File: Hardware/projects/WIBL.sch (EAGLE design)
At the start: 105 parts, among them T2 S8050, T3 S8050, T4 S8050, U1 ESP32-WROOM-32E, U2 TJA1051T/3, U3 LSM6DS3TR-C, U4 AMS1117-3.3, U5 SN65C1168NSR

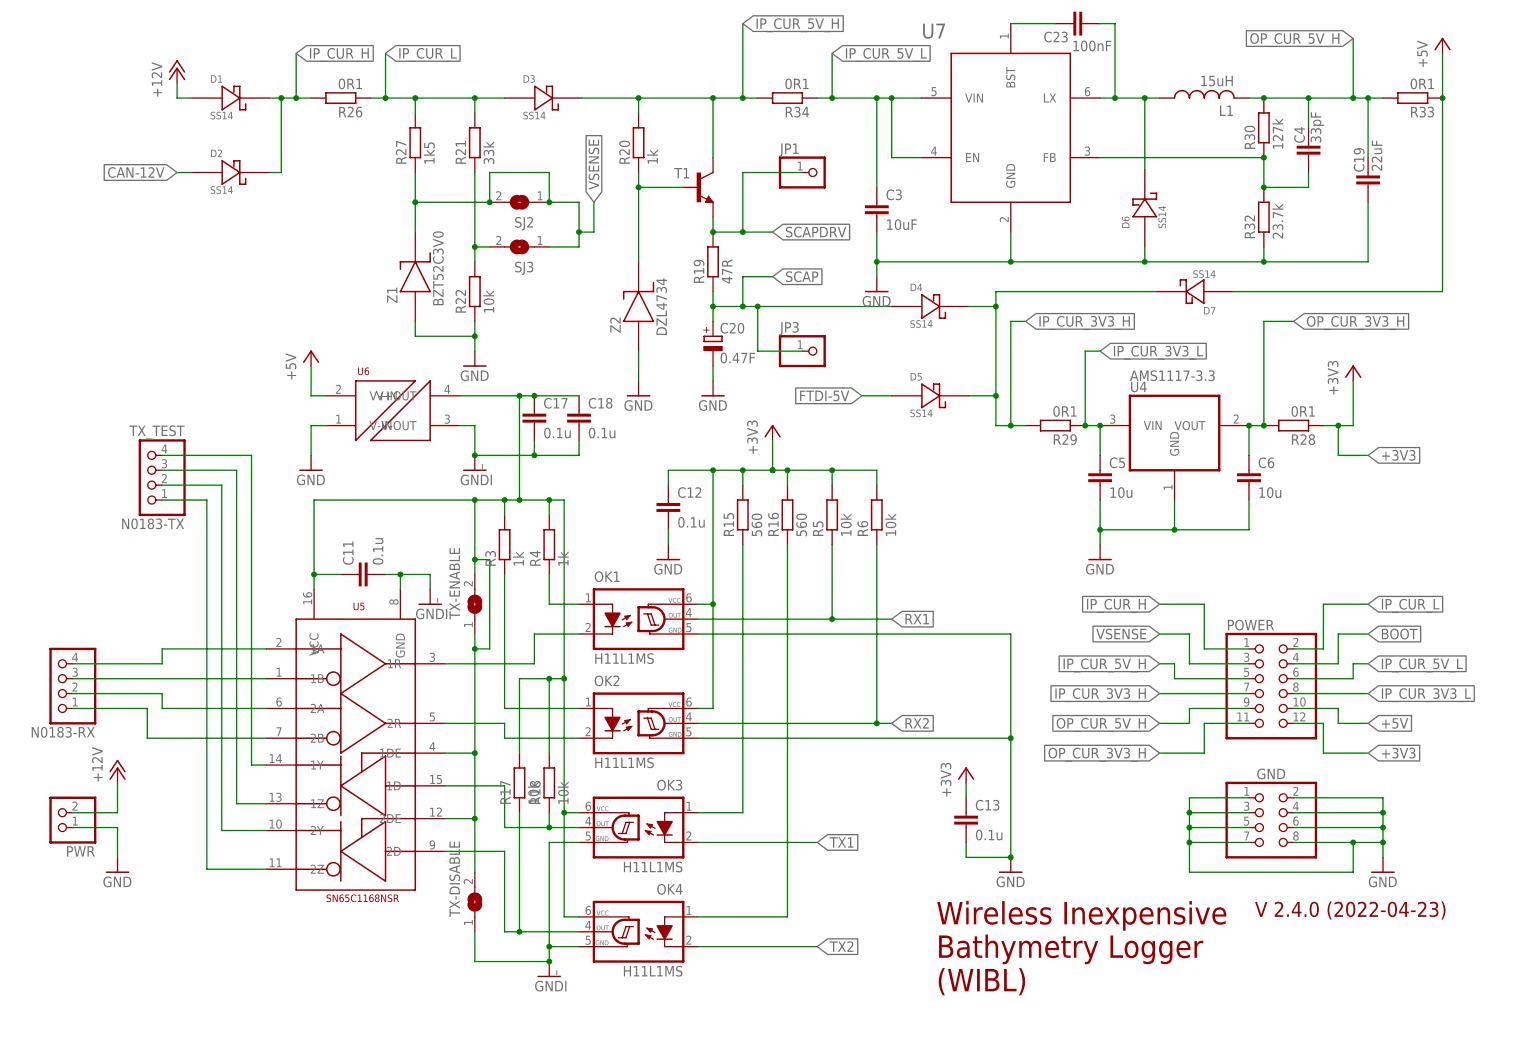
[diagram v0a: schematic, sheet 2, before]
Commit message: Added missing 2.4.1 hardware design files.
For reasons unknown, the v 2.4.1 schematic and board files never got checked into the repository; these are from a backup copy that reflects the initial state.
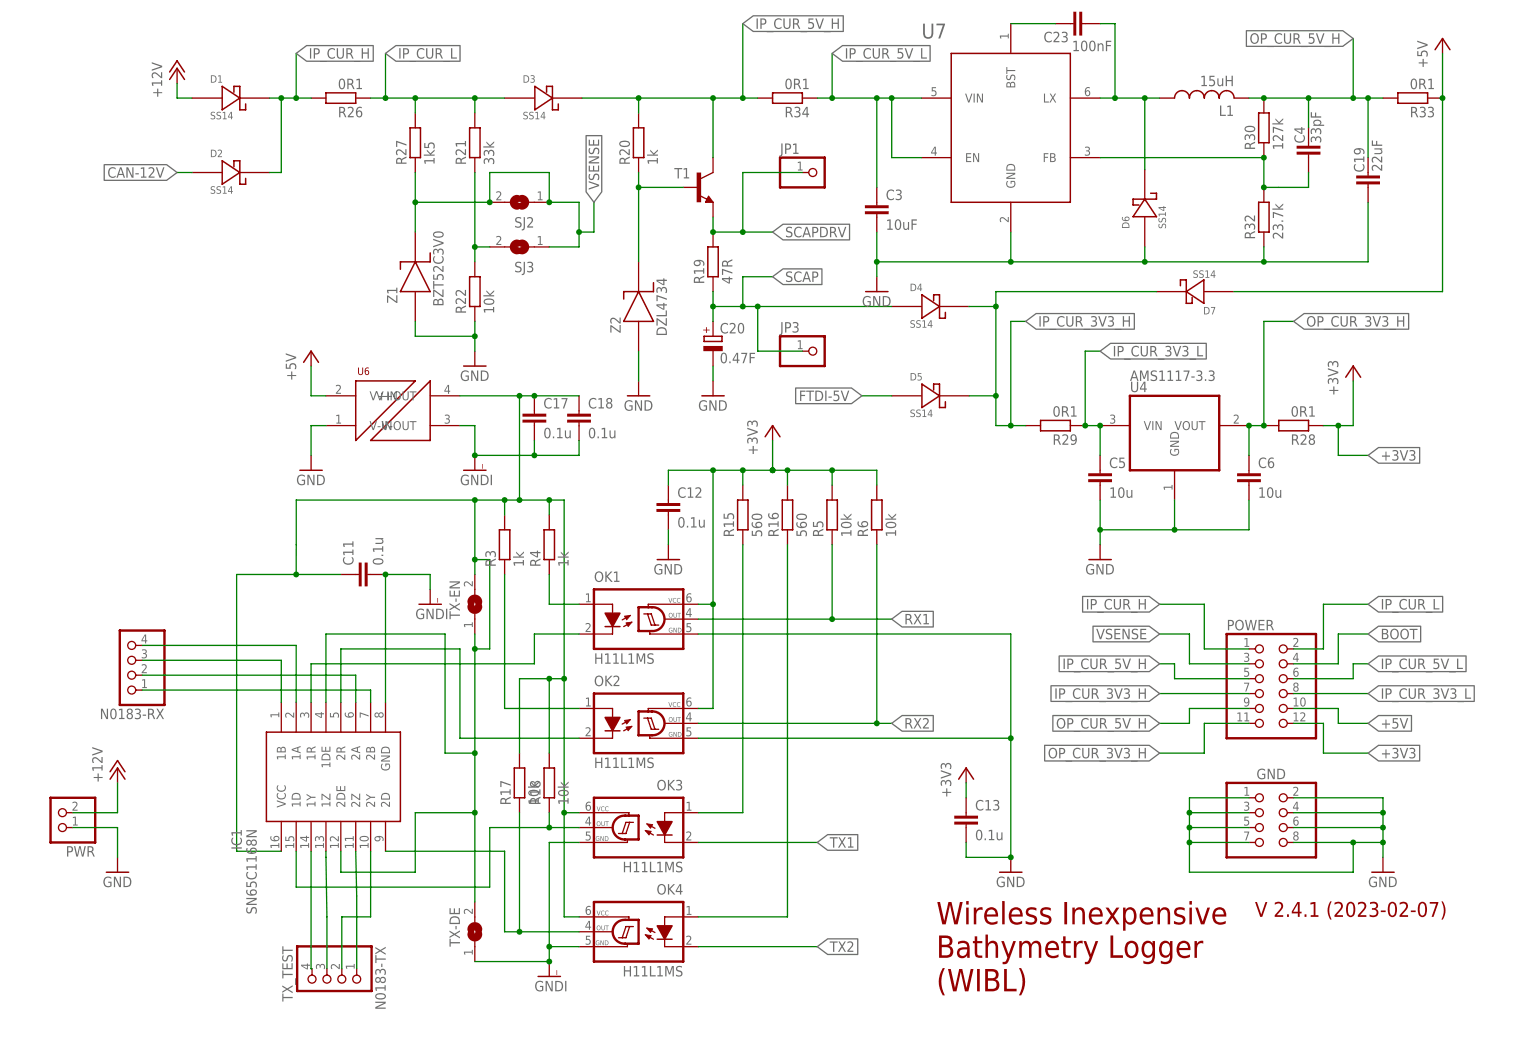
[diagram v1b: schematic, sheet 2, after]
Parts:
- removed TX-DISABLE: (no value), jumper:SJ
- removed U5: SN65C1168NSR, sb2030_logger:SN65C1168-SOIC
- added IC1: SN65C1168N, SN65C1168N:SN65C1168N
- added TX-DE: (no value), jumper:SJ
- renumbered TX-ENABLE to TX-EN
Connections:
- removed net N$27: N0183-TX.4, U5.1Y
- removed net N$28: N0183-TX.3, U5.1Z
- removed net N$29: N0183-TX.2, U5.2Y
- removed net N$30: N0183-TX.1, U5.2Z
- new net N$12: IC1.2A, N0183-RX.2
- new net N$5: IC1.1A, N0183-RX.4
- new net N$8: IC1.1Y, N0183-TX.4
- new net N$9: IC1.1B, N0183-RX.3
- net GNDI: now also IC1.GND, TX-DE.1; no longer TX-DISABLE.1, U5.GND
- net N$13: now also IC1.1R; no longer U5.1R
- net N$14: now also IC1.2R; no longer U5.2R
- net N$17: now also IC1.2B, N0183-RX.1; no longer N0183-RX.4, U5.1A
- net N$18: now also IC1.1Z, N0183-TX.3; no longer N0183-RX.3, U5.1B
- net N$19: now also IC1.2Y, N0183-TX.2; no longer N0183-RX.2, U5.2A
- net N$20: now also IC1.2Z, N0183-TX.1; no longer N0183-RX.1, U5.2B
- net N$21: now also IC1.1DE, IC1.2DE, IC1.VCC, TX-DE.2; no longer TX-DISABLE.2, U5.1DE, U5.2DE, U5.VCC
- net N$33: now also IC1.1D; no longer U5.1D
- net N$34: now also IC1.2D; no longer U5.2D
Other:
- note added: "V 2.4.1 (2023-02-07)"
- note added: "V2.4.1 (2023-02-07)"
- note removed: "V 2.4.0 (2022-04-23)"
- note removed: "V2.4.0 (2022-04-23)"
- moved on the sheet: N0183-RX, N0183-TX

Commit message: Restore accidentally deleted files
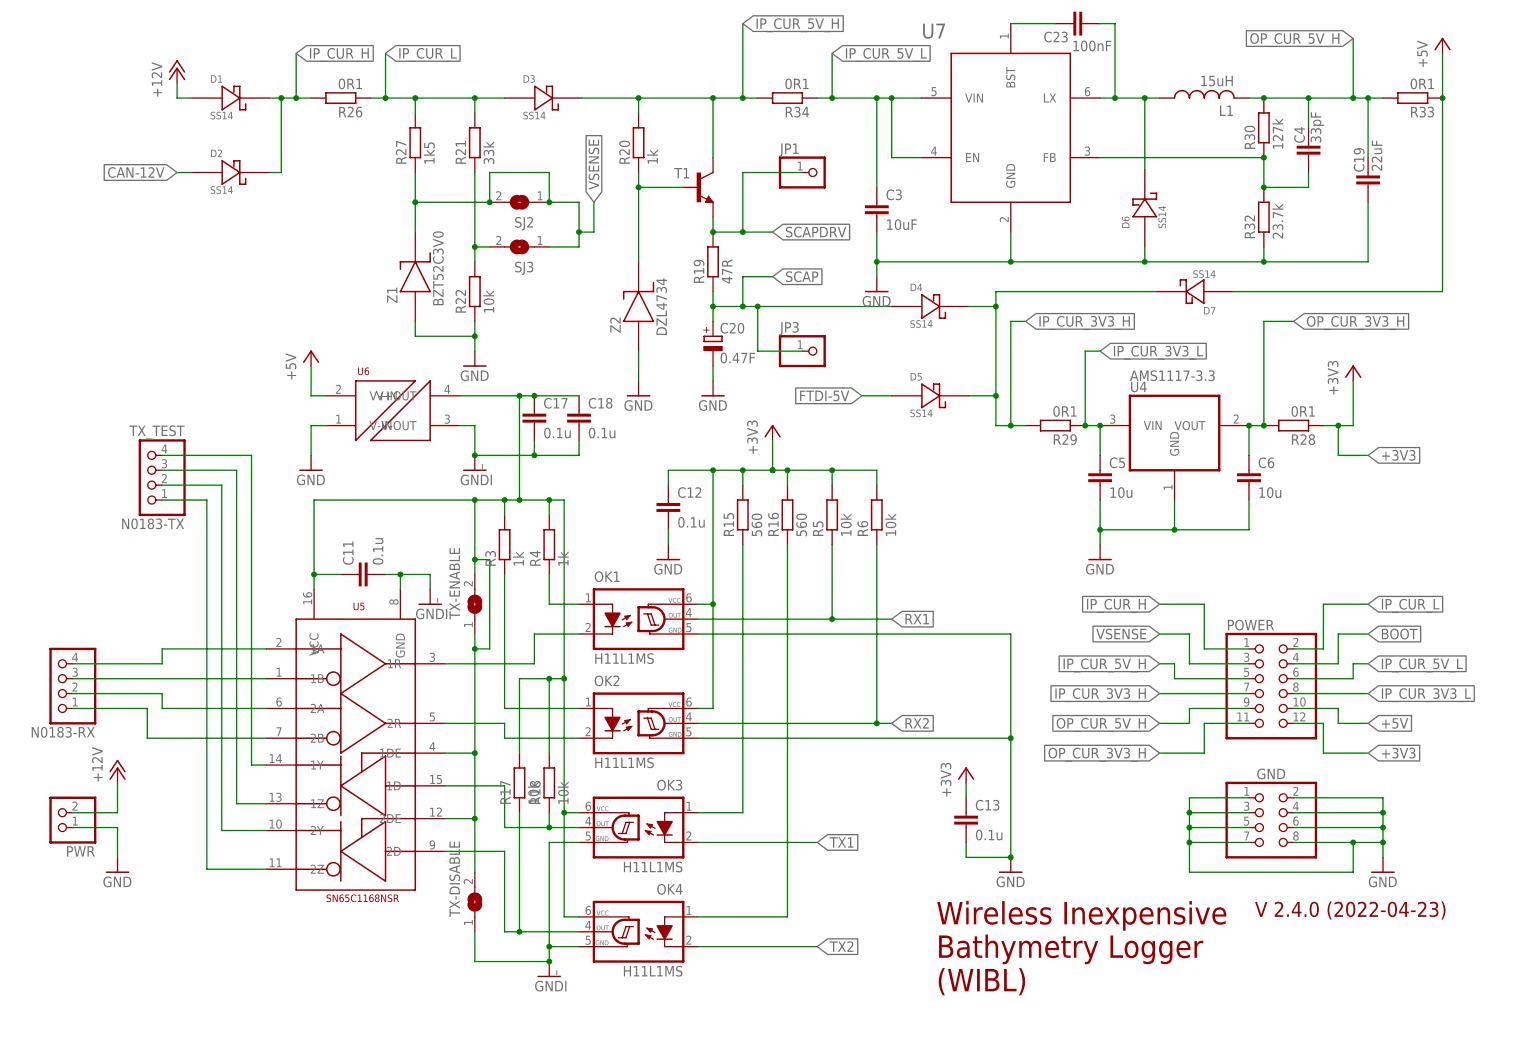
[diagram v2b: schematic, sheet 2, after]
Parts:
- removed IC1: SN65C1168N, SN65C1168N:SN65C1168N
- removed TX-DE: (no value), jumper:SJ
- added TX-DISABLE: (no value), jumper:SJ
- added U5: SN65C1168NSR, sb2030_logger:SN65C1168-SOIC
- renumbered TX-EN to TX-ENABLE
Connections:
- removed net N$12: IC1.2A, N0183-RX.2
- removed net N$5: IC1.1A, N0183-RX.4
- removed net N$8: IC1.1Y, N0183-TX.4
- removed net N$9: IC1.1B, N0183-RX.3
- new net N$27: N0183-TX.4, U5.1Y
- new net N$28: N0183-TX.3, U5.1Z
- new net N$29: N0183-TX.2, U5.2Y
- new net N$30: N0183-TX.1, U5.2Z
- net GNDI: now also TX-DISABLE.1, U5.GND; no longer IC1.GND, TX-DE.1
- net N$13: now also U5.1R; no longer IC1.1R
- net N$14: now also U5.2R; no longer IC1.2R
- net N$17: now also N0183-RX.4, U5.1A; no longer IC1.2B, N0183-RX.1
- net N$18: now also N0183-RX.3, U5.1B; no longer IC1.1Z, N0183-TX.3
- net N$19: now also N0183-RX.2, U5.2A; no longer IC1.2Y, N0183-TX.2
- net N$20: now also N0183-RX.1, U5.2B; no longer IC1.2Z, N0183-TX.1
- net N$21: now also TX-DISABLE.2, U5.1DE, U5.2DE, U5.VCC; no longer IC1.1DE, IC1.2DE, IC1.VCC, TX-DE.2
- net N$33: now also U5.1D; no longer IC1.1D
- net N$34: now also U5.2D; no longer IC1.2D
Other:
- note added: "V 2.4.0 (2022-04-23)"
- note added: "V2.4.0 (2022-04-23)"
- note removed: "V 2.4.1 (2023-02-07)"
- note removed: "V2.4.1 (2023-02-07)"
- moved on the sheet: N0183-RX, N0183-TX
